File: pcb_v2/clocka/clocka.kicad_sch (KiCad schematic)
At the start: 44 parts, among them J26 bus clock, SW1 RESET, SW2 RESET, SW3 RESET, SW4 RESET, SW5 RESET, SW6 RESET, SW7 CLOCK_SELECT, U1 74LS74, U2 74LS74, U3 74LS74, U4 74LS04, U5 74LS125

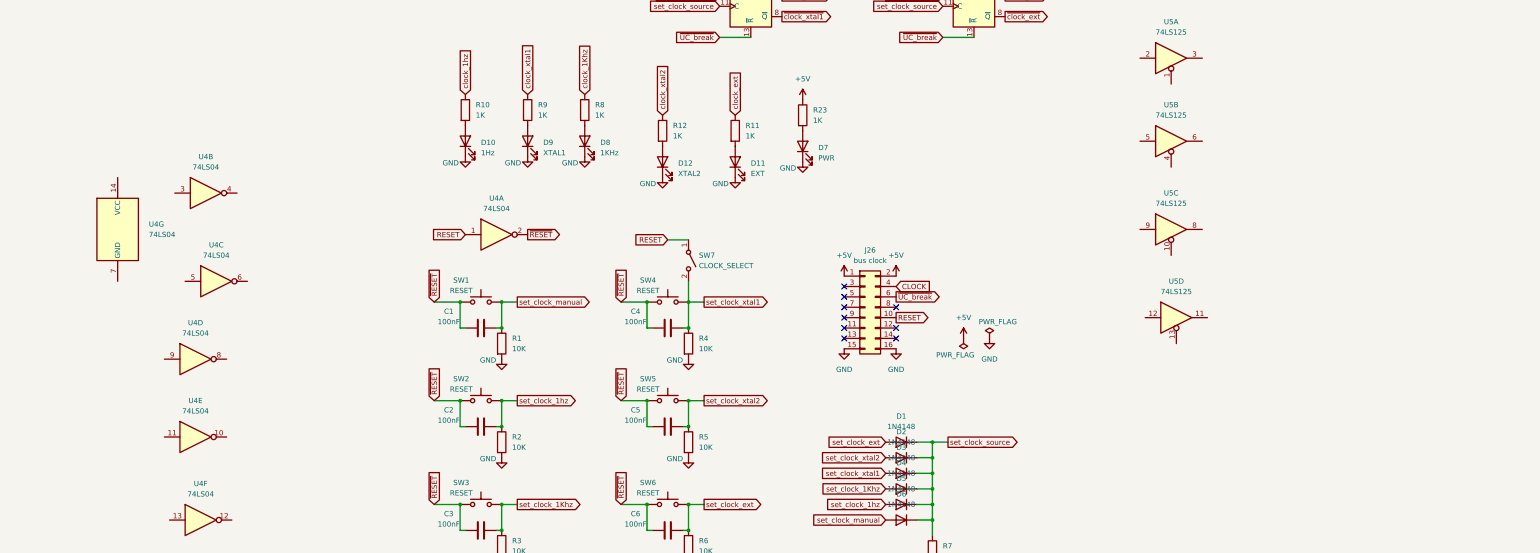
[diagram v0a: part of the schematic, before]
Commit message: placa clock gerando os sinais clock e n_clock sincronizados
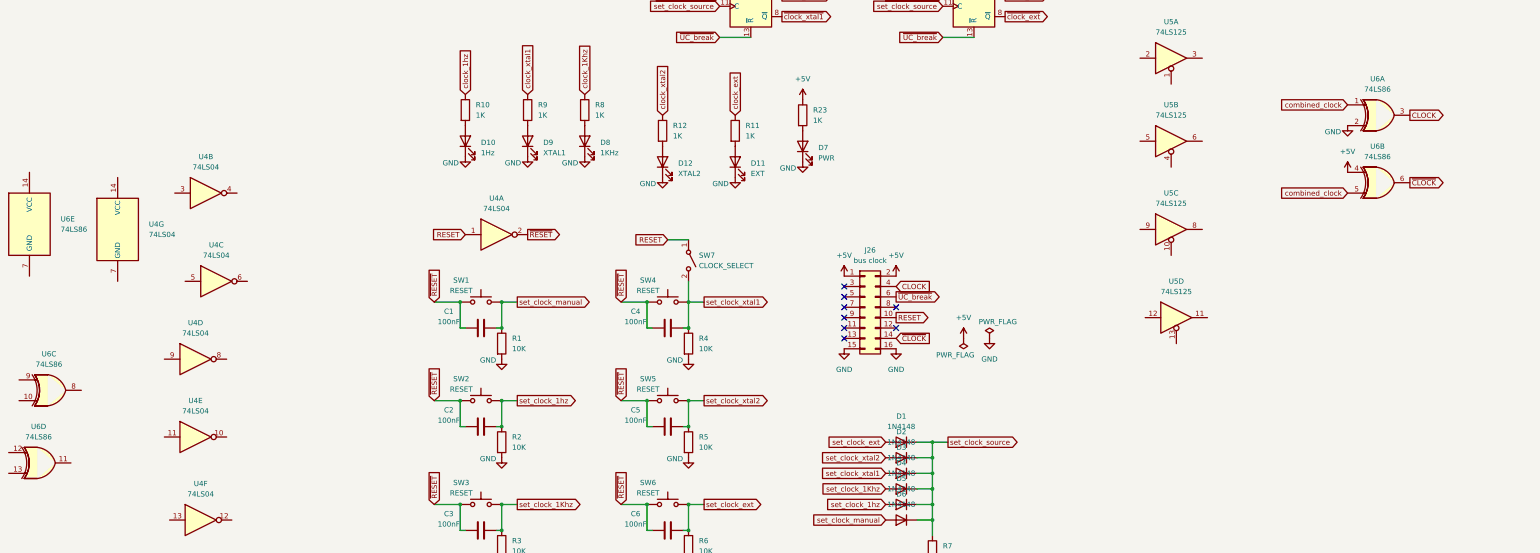
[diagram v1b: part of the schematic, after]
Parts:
- added U6: 74LS86, symbol 74xx:74LS86
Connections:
- net +5V: now also U6.4
- net CLOCK: now also U6.3
- net GND: now also U6.2
- net ~{CLOCK}: now reaches J26.14 (Pin_14)
- net ~{CLOCK}: now also U6.6
- new net combined_clock: U6.1, U6.5
- no-connect marks 9 -> 8

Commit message: adicionados os botões para clock manual
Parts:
- added C10, C11, C14, C8, C9: 10nF, Capacitor_THT:C_Disc_D4.7mm_W2.5mm_P5.00mm, symbol Device:C
- added C12, C13: 100nF, Capacitor_THT:C_Disc_D4.7mm_W2.5mm_P5.00mm, symbol Device:C
- added C7: 10uF, symbol Device:C_Polarized
- added D13, D14, D15, D16, D17, D18, D20: 1N4148, Diode_THT:D_DO-35_SOD27_P7.62mm_Horizontal, symbol Diode:1N4148
- added D19: CLOCK PULSE, LED_THT:LED_D5.0mm, symbol Device:LED
- added J1: clock_ext, symbol Connector_Generic:Conn_01x02
- added R13, R15, R25: 1K, Resistor_THT:R_Axial_DIN0207_L6.3mm_D2.5mm_P7.62mm_Horizontal, symbol Device:R
- added R14, R16: 68K, Resistor_THT:R_Axial_DIN0207_L6.3mm_D2.5mm_P7.62mm_Horizontal, symbol Device:R
- added R17, R18, R19, R21, R24: 10K, Resistor_THT:R_Axial_DIN0207_L6.3mm_D2.5mm_P7.62mm_Horizontal, symbol Device:R
- added R20, R22: 2K2, Resistor_THT:R_Axial_DIN0207_L6.3mm_D2.5mm_P7.62mm_Horizontal, symbol Device:R
- added RV1, RV2: 20K, symbol Device:R_Potentiometer_Trim
- added SW8: HALF STEP, Button_Switch_THT:SW_PUSH_6mm, symbol Switch:SW_Push
- added SW9: STEP, Button_Switch_THT:SW_PUSH_6mm, symbol Switch:SW_Push
- added U10: 74LS125, symbol 74xx:74LS125
- added U11, U12, U8, U9: NE555P, Package_DIP:DIP-8_W7.62mm, symbol Timer:NE555P
- added U7: 74LS08, symbol 74xx:74LS08
- added Y1: 400KHz, Oscillator:Oscillator_DIP-8, symbol Oscillator:CXO_DIP8
- added Y2: 1MHz, Oscillator:Oscillator_DIP-8, symbol Oscillator:CXO_DIP8
- SW1: value RESET -> MANUAL
- SW2: value RESET -> 1HZ
- SW3: value RESET -> 1KHZ
- SW4: value RESET -> XTAL1
- SW5: value RESET -> XTAL2
- SW6: value RESET -> EXT
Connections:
- net +5V: now also R1.1, R13.1, R15.1, R19.2, R20.1, R21.2, R22.1, U11.4 (~{RST}), U11.8 (VCC), U12.4 (~{RST}), U12.8 (VCC), U8.4 (~{RST}), U8.8 (VCC), U9.4 (~{RST}), U9.8 (VCC), Y1.1 (EN), Y1.8 (Vcc), Y2.1 (EN), Y2.8 (Vcc)
- net GND: now also U1.4 (~{S}), U6.10, C10.2, C11.2, C12.1, C13.1, C14.2, C7.2, C8.2, C9.1, D19.1 (K), J1.1 (Pin_1), R17.2, R18.2, R24.1, SW8.1, SW9.1, U11.1 (GND), U12.1 (GND), U8.1 (GND), U9.1 (GND), Y1.4 (GND), Y2.4 (GND); no longer R1.2
- net RESET: no longer U4.1
- net clock_1Khz: now also D13.2 (A)
- net clock_1hz: now also D6.2 (A)
- net clock_ext: now also D16.2 (A)
- net clock_xtal1: now also D14.2 (A)
- net clock_xtal2: now also D15.2 (A)
- net combined_clock: now also U5.11, U5.3, U5.6, U5.8, U6.9, U10.3, U10.6
- net set_clock_source: no longer D6.1 (K)
- net ~{clock_1Khz}: now also U5.4
- net ~{clock_1hz}: now also U5.1
- net ~{clock_ext}: now also U10.1
- net ~{clock_xtal1}: now also U5.10
- net ~{clock_xtal2}: now also U5.13
- net at U4.10: now also C4.1, SW4.1
- net signal_xtal1: now reaches U4.11
- net signal_xtal1: now also U5.9, Y1.5 (OUT)
- net signal_1Hz: now reaches U5.2
- net signal_1Hz: now also U4.1, D20.2 (A), U8.3 (OUT)
- net signal_xtal2: now reaches U4.5
- net signal_xtal2: now also U5.12, Y2.5 (OUT)
- net at U4.6: now also C5.1, SW5.1
- net ~{reset}: now reaches U1.1 (~{R})
- net at U1.2 (D): now also U1.6 (~{Q})
- net at U1.3 (C): now also U11.3 (OUT)
- net at U1.5 (Q): now also D17.2 (A)
- net signal_1KHz: now reaches U5.5
- net signal_1KHz: now also U4.3, U9.3 (OUT)
- net at U4.4: now also C3.1, SW3.1
- net at U4.8: now also C6.1, SW6.1
- net signal_ext: now reaches U4.9
- net signal_ext: now also J1.2 (Pin_2), R17.1, U10.2
- net ~{clock_manual}: now reaches U4.12
- net ~{clock_manual}: now also U10.4
- net at U4.13: now also D6.1 (K), D13.1 (K), D14.1 (K), D15.1 (K), D16.1 (K), R18.1
- net ~{operator_break_enable}: now reaches U6.8
- net ~{operator_break_enable}: now also C1.1, SW1.1
- net set_clock_manual renamed ~{operator_break}
- net ~{operator_break}: now also R1.2, U7.1; no longer D6.2 (A), R1.1
- removed net ~{RESET}: C1.1, C2.1, C3.1, C4.1, C5.1, C6.1, SW1.1, SW2.1, SW3.1, SW4.1, SW5.1, SW6.1, U4.2
- net ~{UC_break} renamed ~{disengage_clock}
- net ~{disengage_clock}: now also U7.3; no longer J26.6 (Pin_6)
- new net: C9.2, RV2.3, U9.2 (TRIG), U9.6 (THRES)
- new net: C10.1, U9.5 (CONT)
- new net: R15.2, R16.2, U9.7 (DISCH)
- new net: C2.1, SW2.1, U4.2
- new net: R14.1, RV1.2
- new net: C7.1, RV1.3, U8.2 (TRIG), U8.6 (THRES)
- new net: C13.2, R22.2, U12.6 (THRES), U12.7 (DISCH)
- new net: D17.1 (K), D18.1 (K), D20.1 (K), R24.2, R25.1, U10.5
- new net: C11.1, U11.5 (CONT)
- new net: C8.1, U8.5 (CONT)
- new net: R16.1, RV2.2
- new net: R19.1, SW8.2, U11.2 (TRIG)
- new net: C12.2, R20.2, U11.6 (THRES), U11.7 (DISCH)
- new net: R21.1, SW9.2, U12.2 (TRIG)
- new net: D19.2 (A), R25.2
- new net: C14.1, U12.5 (CONT)
- new net: D18.2 (A), U12.3 (OUT)
- new net: R13.2, R14.2, U8.7 (DISCH)
- new net ~{control_break}: J26.6 (Pin_6), U7.2
- no-connect marks 8 -> 10
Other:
- moved on the sheet: C1, C2, C3, C4, C5, C6, D1, D10, D11, D12, D2, D3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

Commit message: concluído o esquemático do clock; iniciando o layout do pcb a partir das dimensões definidas no croqui
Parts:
- removed R19: 10K, Resistor_THT:R_Axial_DIN0207_L6.3mm_D2.5mm_P7.62mm_Horizontal, symbol Device:R
- removed R20: 2K2, Resistor_THT:R_Axial_DIN0207_L6.3mm_D2.5mm_P7.62mm_Horizontal, symbol Device:R
- removed RV2: 20K, symbol Device:R_Potentiometer_Trim
- added C15, C17, C19, C20, C21, C22, C23, C24, C25, C26, C28: 100nF, Capacitor_THT:C_Disc_D4.7mm_W2.5mm_P5.00mm, symbol Device:C
- added C27: 10nF, Capacitor_THT:C_Disc_D4.7mm_W2.5mm_P5.00mm, symbol Device:C
- added R26: 1K, Resistor_THT:R_Axial_DIN0207_L6.3mm_D2.5mm_P7.62mm_Horizontal, symbol Device:R
- added R27: 68K, Resistor_THT:R_Axial_DIN0207_L6.3mm_D2.5mm_P7.62mm_Horizontal, symbol Device:R
- added RV3: 20K, Potentiometer_THT:Potentiometer_ACP_CA9-H5_Horizontal, symbol Device:R_Potentiometer_Trim
- C14: value 10nF -> 100nF
- C7: footprint (none) -> Capacitor_THT:CP_Radial_D5.0mm_P2.50mm
- J1, SW7: footprint (none) -> Connector_Molex:Molex_KK-254_AE-6410-02A_1x02_P2.54mm_Vertical
- R15: value 1K -> 10K
- R16: value 68K -> 2K2
- RV1: footprint (none) -> Potentiometer_THT:Potentiometer_ACP_CA9-H5_Horizontal
- SW8: value HALF STEP -> HALF-STEP
- U1, U10, U2, U3, U4, U5, U6, U7: footprint (none) -> Package_DIP:DIP-14_W7.62mm
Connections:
- net +5V: now also C12.2, R15.2, R16.1, U1.14 (VCC), U10.10, U10.12, U10.13, U10.14 (VCC), U10.9, U2.14 (VCC), U3.14 (VCC), U4.14 (VCC), U5.14 (VCC), U6.12, U6.13, U6.14 (VCC), U7.10, U7.12, U7.13, U7.14 (VCC), U7.4, U7.5, U7.9, C15.2, C17.1, C19.2, C20.2, C21.2, C22.2, C23.2, C24.2, C25.2, C26.2, C28.1, R26.1; no longer R15.1
- net GND: now also C10.1, C11.1, C14.1, C8.1, U1.7 (GND), U10.7 (GND), U2.7 (GND), U3.7 (GND), U4.7 (GND), U5.7 (GND), U6.7 (GND), U7.7 (GND), C15.1, C17.2, C19.1, C20.1, C21.1, C22.1, C23.1, C24.1, C25.1, C26.1, C27.1, C28.2; no longer C10.2, C11.2, C14.2, C8.2
- net RESET: now also U4.13
- net ~{clock_manual}: now also D13.1 (K), D14.1 (K), D15.1 (K), D16.1 (K), D6.1 (K), R18.1; no longer U4.12
- net ~{reset}: now also U4.12
- net at C9.2, U9.2 (TR), U9.6 (THR): now also RV3.2
- net at U9.5 (CV): now also C27.2; no longer C10.1
- net at U1.3 (C): now also U12.3 (Q); no longer U11.3 (OUT)
- net at RV1.1: now also R14.1
- net at RV1.2: now also C7.1, U8.2 (TR), U8.6 (THR); no longer R14.1
- net at C13.2, R22.2: now also U11.6 (THR), U11.7 (DIS); no longer U12.6 (THRES), U12.7 (DISCH)
- net at U11.5 (CV): now also C10.2; no longer C11.1
- net at U8.5 (CV): now also C8.2; no longer C8.1
- net at SW8.2: now also R15.1, U12.2 (TR); no longer U11.2 (TRIG)
- net at R21.1, SW9.2: now also U11.2 (TR); no longer U12.2 (TRIG)
- net at U12.5 (CV): now also C11.2; no longer C14.1
- net at D18.2 (A): now also U11.3 (Q); no longer U12.3 (OUT)
- new net: R26.2, R27.2, U9.7 (DIS)
- new net: C14.2, R16.2, U12.6 (THR), U12.7 (DIS)
- new net: R27.1, RV3.1
- now unconnected: RV1.3
- no-connect marks 10 -> 16
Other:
- moved on the sheet: C13, C7, C8, C9, D18, J1, R13, R14, R17, R21, R22, R24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

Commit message: Separado o painel de controle do gerador de clock
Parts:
- removed C1, C2, C3, C4, C5, C6: 100nF, Capacitor_THT:C_Disc_D4.7mm_W2.5mm_P5.00mm, symbol Device:C
- removed C10, C11, C8, C9: 10nF, Capacitor_THT:C_Disc_D4.7mm_W2.5mm_P5.00mm, symbol Device:C
- removed C7: 10uF, Capacitor_THT:CP_Radial_D5.0mm_P2.50mm, symbol Device:C_Polarized
- removed D10: 1Hz, LED_THT:LED_D5.0mm, symbol Device:LED
- removed D11: EXT, LED_THT:LED_D5.0mm, symbol Device:LED
- removed D12: XTAL2, LED_THT:LED_D5.0mm, symbol Device:LED
- removed D8: 1KHz, LED_THT:LED_D5.0mm, symbol Device:LED
- removed D9: XTAL1, LED_THT:LED_D5.0mm, symbol Device:LED
- removed R10, R11, R12, R8, R9: 1K, Resistor_THT:R_Axial_DIN0207_L6.3mm_D2.5mm_P7.62mm_Horizontal, symbol Device:R
- added C15, C16, C17, C18, C19, C20: 100nF, Capacitor_THT:C_Disc_D4.7mm_W2.5mm_P5.00mm, symbol Device:C
- added C21, C22, C23, C24: 10nF, Capacitor_THT:C_Disc_D4.7mm_W2.5mm_P5.00mm, symbol Device:C
- added C25: 10uF, Capacitor_THT:CP_Radial_D5.0mm_P2.50mm, symbol Device:C_Polarized
- SW1: value MANUAL -> BREAK; footprint Button_Switch_THT:SW_PUSH_6mm -> Connector_JST:JST_XH_B2B-XH-AM_1x02_P2.50mm_Vertical
- SW2, SW3, SW4, SW5, SW6, SW8, SW9: footprint Button_Switch_THT:SW_PUSH_6mm -> Connector_JST:JST_XH_B2B-XH-AM_1x02_P2.50mm_Vertical
- SW7: value CLOCK_SELECT -> CLOCK_RESET; footprint Connector_Molex:Molex_KK-254_AE-6410-02A_1x02_P2.54mm_Vertical -> Connector_JST:JST_XH_B2B-XH-AM_1x02_P2.50mm_Vertical
- renumbered C21 to C1, C25 to C10, C15 to C11, C20 to C2, C19 to C3, C24 to C4, C22 to C5, C23 to C6, C26 to C7, C17 to C8, C28 to C9
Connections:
- net +5V: no longer U7.10, U7.4, U7.5, U7.9
- net GND: now also C21.1, C22.1, C23.1, C24.1, C25.2
- net set_clock_1Khz: now also C17.2
- net set_clock_1hz: now also C16.2
- net set_clock_ext: now also C19.2
- net set_clock_source: now also U7.8; no longer D1.1 (K), D2.1 (K), D3.1 (K), D4.1 (K), D5.1 (K), R7.1
- net set_clock_xtal1: now also C20.2
- net set_clock_xtal2: now also C18.2
- net ~{operator_break_enable}: now also C15.1
- net ~{operator_break}: now also C15.2
- net at SW4.1, U4.10: now also C20.1
- net at U12.5 (CV): now also C22.2
- net at SW5.1, U4.6: now also C18.1
- net at SW2.1, U4.2: now also C16.1
- net at RV1.2, U8.2 (TR), U8.6 (THR): now also C25.1
- net at U8.5 (CV): now also C23.2
- net at RV3.2, U9.2 (TR), U9.6 (THR): now also C21.2
- net at SW3.1, U4.4: now also C17.1
- net at SW6.1, U4.8: now also C19.1
- net at U11.5 (CV): now also C24.2
- net at U7.6: now also U7.10, U7.9
- new net: D1.1 (K), D2.1 (K), D3.1 (K), D4.1 (K), D5.1 (K), R7.1, U7.4, U7.5
- no-connect marks 16 -> 14
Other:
- moved on the sheet: D1, D2, D3, D4, D5, R7, U6D, U7B, U7C, U7D

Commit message: layout do painel de controle do gerador de clock
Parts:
- removed C15, C16, C17, C18, C19, C20: 100nF, Capacitor_THT:C_Disc_D4.7mm_W2.5mm_P5.00mm, symbol Device:C
- removed D19: CLOCK PULSE, LED_THT:LED_D5.0mm, symbol Device:LED
- removed J1: clock_ext, Connector_Molex:Molex_KK-254_AE-6410-02A_1x02_P2.54mm_Vertical, symbol Connector_Generic:Conn_01x02
- removed R1, R17, R2, R3, R4, R5, R6: 10K, Resistor_THT:R_Axial_DIN0207_L6.3mm_D2.5mm_P7.62mm_Horizontal, symbol Device:R
- removed R25: 1K, Resistor_THT:R_Axial_DIN0207_L6.3mm_D2.5mm_P7.62mm_Horizontal, symbol Device:R
- removed SW1: BREAK, Connector_JST:JST_XH_B2B-XH-AM_1x02_P2.50mm_Vertical, symbol Switch:SW_Push
- removed SW2: 1HZ, Connector_JST:JST_XH_B2B-XH-AM_1x02_P2.50mm_Vertical, symbol Switch:SW_Push
- removed SW3: 1KHZ, Connector_JST:JST_XH_B2B-XH-AM_1x02_P2.50mm_Vertical, symbol Switch:SW_Push
- removed SW4: XTAL1, Connector_JST:JST_XH_B2B-XH-AM_1x02_P2.50mm_Vertical, symbol Switch:SW_Push
- removed SW5: XTAL2, Connector_JST:JST_XH_B2B-XH-AM_1x02_P2.50mm_Vertical, symbol Switch:SW_Push
- removed SW6: EXT, Connector_JST:JST_XH_B2B-XH-AM_1x02_P2.50mm_Vertical, symbol Switch:SW_Push
- removed SW7: CLOCK_RESET, Connector_JST:JST_XH_B2B-XH-AM_1x02_P2.50mm_Vertical, symbol Switch:SW_SPST
- removed SW8: HALF-STEP, Connector_JST:JST_XH_B2B-XH-AM_1x02_P2.50mm_Vertical, symbol Switch:SW_Push
- removed SW9: STEP, Connector_JST:JST_XH_B2B-XH-AM_1x02_P2.50mm_Vertical, symbol Switch:SW_Push
- added J3: control panel, Connector_PinHeader_2.54mm:PinHeader_2x08_P2.54mm_Vertical, symbol Connector_Generic:Conn_02x08_Odd_Even
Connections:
- net RESET: now also J3.5 (Pin_5)
- net clock_1Khz: now also J3.4 (Pin_4)
- net clock_1hz: now also J3.2 (Pin_2)
- net clock_ext: now also J3.10 (Pin_10)
- net clock_xtal1: now also J3.6 (Pin_6)
- net clock_xtal2: now also J3.8 (Pin_8)
- net set_clock_1Khz: now also J26.13 (Pin_13)
- net set_clock_1hz: now also J26.9 (Pin_9)
- net set_clock_ext: now also J26.14 (Pin_14)
- net set_clock_xtal1: now also J26.6 (Pin_6)
- net set_clock_xtal2: now also J26.10 (Pin_10)
- net signal_ext: now also J3.14 (Pin_14)
- net ~{clock_manual}: now also J3.12 (Pin_12)
- net ~{operator_break_enable}: now also J26.3 (Pin_3)
- net ~{operator_break}: now also J26.5 (Pin_5)
- net at U4.10: now also J26.4 (Pin_4)
- net half_step: now reaches R15.1, U12.2 (TR)
- net half_step: now also J3.3 (Pin_3)
- net at U4.6: now also J26.8 (Pin_8)
- net at U4.2: now also J26.7 (Pin_7)
- net at U4.4: now also J26.11 (Pin_11)
- net clock_pulse: now reaches D17.1 (K), D18.1 (K), D20.1 (K), R24.2, U10.5
- net clock_pulse: now also J3.16 (Pin_16)
- net at U4.8: now also J26.12 (Pin_12)
- net step: now reaches R21.1, U11.2 (TR)
- net step: now also J3.1 (Pin_1)
- no-connect marks 14 -> 19
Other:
- moved on the sheet: D7, J2, R23, U4A, U4B, U4C, U4D, U4E

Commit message: layout de pcb do clock
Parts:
- removed C25: 10uF, Capacitor_THT:CP_Radial_D5.0mm_P2.50mm, symbol Device:C_Polarized
- removed R15, R21: 10K, Resistor_THT:R_Axial_DIN0207_L6.3mm_D2.5mm_P7.62mm_Horizontal, symbol Device:R
- added C15: 10uF, Capacitor_THT:C_Disc_D4.7mm_W2.5mm_P5.00mm, symbol Device:C
- added J26: bus clock, Connector_PinHeader_2.54mm:PinHeader_2x08_P2.54mm_Vertical, symbol Connector_Generic:Conn_02x08_Odd_Even
- J2: renamed from J26; value bus clock -> control panel
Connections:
- net +5V: now also J26.1 (Pin_1), J26.2 (Pin_2)
- net CLOCK: now also J3.7 (Pin_7), J26.4 (Pin_4); no longer J2.4 (Pin_4)
- net GND: now also C15.1, J26.15 (Pin_15), J26.16 (Pin_16)
- net RESET: now also J26.10 (Pin_10); no longer J2.10 (Pin_10)
- net clock_pulse: now also J3.9 (Pin_9); no longer J3.16 (Pin_16)
- net half_step: now also J3.1 (Pin_1); no longer J3.3 (Pin_3)
- net set_clock_1Khz: now also J2.14 (Pin_14); no longer J2.13 (Pin_13)
- net set_clock_1hz: now also J2.13 (Pin_13); no longer J2.9 (Pin_9)
- net set_clock_ext: now also J2.9 (Pin_9); no longer J2.14 (Pin_14)
- net set_clock_xtal1: now also J2.11 (Pin_11); no longer J2.6 (Pin_6)
- net set_clock_xtal2: now also J2.12 (Pin_12); no longer J2.10 (Pin_10)
- net signal_ext: now also J3.11 (Pin_11); no longer J3.14 (Pin_14)
- net step: now also J3.3 (Pin_3); no longer J3.1 (Pin_1)
- net ~{CLOCK}: now also J26.14 (Pin_14); no longer J2.14 (Pin_14)
- net ~{control_break}: now also J26.6 (Pin_6); no longer J2.6 (Pin_6)
- net ~{operator_break_enable}: now also J2.7 (Pin_7); no longer J2.3 (Pin_3)
- net ~{operator_break}: now also J2.10 (Pin_10); no longer J2.5 (Pin_5)
- net at U4.10: now also J2.6 (Pin_6); no longer J2.4 (Pin_4)
- net at J2.8 (Pin_8): now also U4.8; no longer U4.6
- net at RV1.2, U8.2 (TR), U8.6 (THR): now also C15.2
- net at RV1.1: no longer R14.1
- net at RV1.3: now also R14.1
- net at U4.4: now also J2.3 (Pin_3); no longer J2.11 (Pin_11)
- net at R27.1: now also RV3.3; no longer RV3.1
- net at U4.2: now also J2.4 (Pin_4); no longer J2.7 (Pin_7)
- net at J2.5 (Pin_5): now also U4.6
- no-connect marks 19 -> 18
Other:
- moved on the sheet: J2, RV1, RV3

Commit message: Novo layout concluído
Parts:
- Y1: value 400KHz -> XTAL1
- Y2: value 1MHz -> XTAL2
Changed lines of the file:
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@@
 		(fields_autoplaced yes)
 		(property "Reference" "Y1"
-			(at 205.74 257.7398 0)
+			(at 204.47 257.7398 0)
 			(effects
 				(font
@@
 			)
 		)
-		(property "Value" "400KHz"
-			(at 205.74 260.2798 0)
+		(property "Value" "XTAL1"
+			(at 204.47 260.2798 0)
 			(effects
 				(font
@@
 			)
 		)
-		(property "Value" "1MHz"
+		(property "Value" "XTAL2"
 			(at 238.76 260.2798 0)
 			(effects

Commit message: continuando implementação do clock
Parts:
- removed D15, D2: 1N4148, Diode_THT:D_DO-35_SOD27_P7.62mm_Horizontal, symbol Diode:1N4148
- removed Y2: XTAL2, Oscillator:Oscillator_DIP-8, symbol Oscillator:CXO_DIP8
- added R1, R2: 1K, Resistor_THT:R_Axial_DIN0207_L6.3mm_D2.5mm_P7.62mm_Horizontal, symbol Device:R
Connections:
- net signal_xtal2 is gone; now on net +5V: U4.5, U5.12
- net +5V: now also U3.1 (~{R}), U3.2 (D), U3.3 (C), U5.13, R2.1
- net GND: now also R1.2
- net RESET: now also R1.1
- net combined_clock: no longer U5.11
- net set_clock_source: no longer U3.3 (C)
- net ~{control_break}: now also R2.2
- net ~{disengage_clock}: no longer U3.1 (~{R})
- net at U4.6: no longer J2.5 (Pin_5)
- net clock_xtal2: no longer names the net of J3.8 (Pin_8)
- net clock_xtal2: no longer U3.5 (Q)
- net set_clock_xtal2: no longer names the net of J2.12 (Pin_12)
- net set_clock_xtal2: no longer U3.2 (D)
- net ~{clock_xtal2}: no longer names the net of U3.6 (~{Q})
- net ~{clock_xtal2}: no longer U5.13
- no-connect marks 18 -> 25
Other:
- moved on the sheet: D16, J2, J3, R18, U10A, U4A, U4B, U4C, U4D, U4E, U5D
